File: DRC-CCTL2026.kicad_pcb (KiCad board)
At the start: 2 copper layers, 80 x 60 mm, 75 parts, among them J1 USB_C, J10 SW3, J12 LCD_BackLight, J2 FDCAN1, J3 FDCAN2, J4 FDCAN3, J5 SW1, J6 SW2, J7 STLINK, J8 I2C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

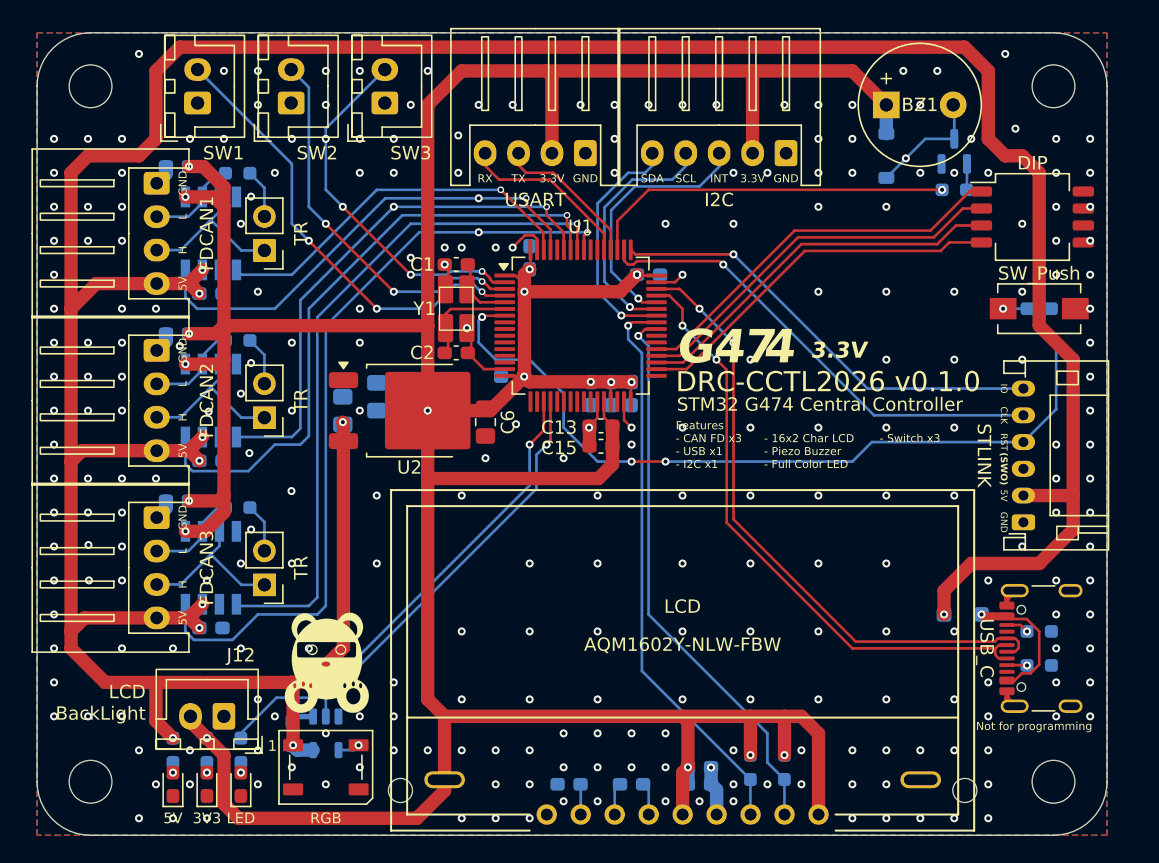
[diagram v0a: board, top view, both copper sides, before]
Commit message: T字配線にフィレットを追加
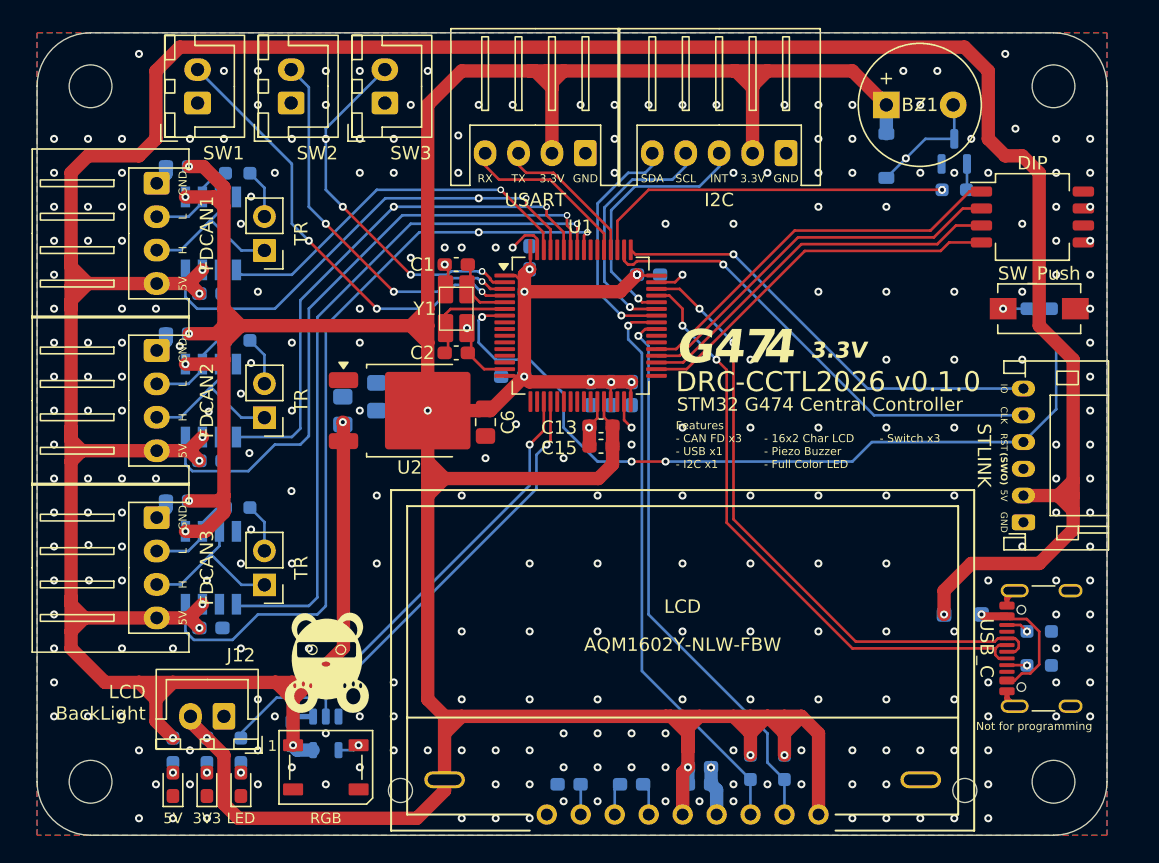
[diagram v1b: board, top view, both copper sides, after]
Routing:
- net +3V3: track 302.0 -> 334.4 mm
- net +5V: track 252.6 -> 271.5 mm

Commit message: 不要なビアを削除
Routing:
- net Net-(BZ1--): vias 1 -> 0
- net /SW3: vias 4 -> 3
- net /FDCAN3_RX: vias 2 -> 1
- net /FDCAN2_TX: vias 2 -> 1
- net /FDCAN1_RX: vias 2 -> 1
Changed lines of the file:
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@@
 		(net 47)
-	)
-	(via
-		(at 174.96 79.39)
-		(size 0.6)
-		(drill 0.3)
-		(layers "F.Cu" "B.Cu")
-		(net 50)
 	)
 	(segment
@@
 		(at 146.576 82.375)
 		(size 0.5)
-		(drill 0.3)
-		(layers "F.Cu" "B.Cu")
-		(net 53)
-	)
-	(via
-		(at 143.02 82.375)
-		(size 0.6)
 		(drill 0.3)
 		(layers "F.Cu" "B.Cu")
@@
 		(net 57)
 	)
-	(via
-		(at 136.67 83.01)
-		(size 0.6)
-		(drill 0.3)
-		(layers "F.Cu" "B.Cu")
-		(net 57)
-	)
 	(segment
 		(start 129.05 100.225)
@@
 		(width 0.2)
 		(layer "F.Cu")
-		(net 62)
-	)
-	(via
-		(at 143.02 84.915)
-		(size 0.6)
-		(drill 0.3)
-		(layers "F.Cu" "B.Cu")
 		(net 62)
 	)
@@
 		(size 0.6)
 		(drill 0.3)
-		(layers "F.Cu" "B.Cu")
-		(net 67)
-	)
-	(via
-		(at 131.59 77.93)
-		(size 0.6)
-		(drill 0.3)

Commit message: 配線を改善
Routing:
- net GND: vias 270 -> 268
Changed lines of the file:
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@@
 	)
 	(via
-		(at 158.26 119.84)
-		(size 0.6)
-		(drill 0.3)
-		(layers "F.Cu" "B.Cu")
-		(free yes)
-		(net 1)
-	)
-	(via
 		(at 118.89 126.19)
 		(size 0.6)
@@
 	)
 	(via
-		(at 162.07 123.65)
-		(size 0.6)
-		(drill 0.3)
-		(layers "F.Cu" "B.Cu")
-		(free yes)
-		(net 1)
-	)
-	(via
 		(at 111.27 90.63)
 		(size 0.6)
@@
 	)
 	(segment
-		(start 155.225 93.945)
-		(end 154.196 92.916)
+		(start 155.225 113.757)
+		(end 155.225 93.945)
 		(width 0.2)
 		(layer "B.Cu")
@@
 	(segment
 		(start 163.34 125.8325)
-		(end 155.225 117.7175)
+		(end 163.34 128.441)
+		(width 0.2)
+		(layer "B.Cu")
+		(net 30)
+	)
+	(segment
+		(start 154.196 92.916)
+		(end 154.196 91.9)
 		(width 0.2)
 		(layer "B.Cu")
@@
 	(segment
 		(start 163.34 125.8325)
-		(end 163.34 128.441)
+		(end 162.451 124.9435)
 		(width 0.2)
 		(layer "B.Cu")
@@
 	)
 	(segment
-		(start 154.196 92.916)
-		(end 154.196 91.9)
+		(start 163.34 128.441)
+		(end 163.35 128.451)
 		(width 0.2)
 		(layer "B.Cu")
@@
 	)
 	(segment
-		(start 155.225 117.7175)
-		(end 155.225 93.945)
+		(start 155.225 93.945)
+		(end 154.196 92.916)
 		(width 0.2)
 		(layer "B.Cu")
@@
 	)
 	(segment
-		(start 163.34 128.441)
-		(end 163.35 128.451)
+		(start 162.451 124.9435)
+		(end 162.451 120.983)
+		(width 0.2)
+		(layer "B.Cu")
+		(net 30)
+	)
+	(segment
+		(start 162.451 120.983)
+		(end 155.225 113.757)
 		(width 0.2)
 		(layer "B.Cu")

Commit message: ledの抵抗値を変更
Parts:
- R3, R5: value 1k -> 470
- R4: value 2.2k -> 1k
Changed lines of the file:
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@@
 			)
 		)
-		(property "Value" "1k"
+		(property "Value" "470"
 			(at 0 -1.43 90)
 			(layer "B.Fab")
@@
 			)
 		)
-		(property "Value" "2.2k"
+		(property "Value" "1k"
 			(at 0 -1.43 90)
 			(layer "B.Fab")
@@
 			)
 		)
-		(property "Value" "1k"
+		(property "Value" "470"
 			(at 0 -1.43 90)
 			(layer "B.Fab")

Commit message: バージョンを変更
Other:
- board text added: "DRC-CCTL2026 v0.0.1"
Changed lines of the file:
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@@
 		)
 	)
-	(gr_text "DRC-CCTL2026 v0.1.0\n"
+	(gr_text "DRC-CCTL2026 v0.0.1"
 		(at 157.752 96.98 0)
 		(layer "F.SilkS")
@@
 			(justify left bottom)
 		)
-		(render_cache "DRC-CCTL2026 v0.1.0\n" 0
+		(render_cache "DRC-CCTL2026 v0.0.1" 0
 			(polygon
 				(pts
@@
 			(polygon
 				(pts
-					(xy 177.971735 96.78948) (xy 177.987118 96.786546) (xy 177.997903 96.777735) (xy 178.003243 96.758064)
-					(xy 178.003243 96.648796) (xy 177.999831 96.625451) (xy 177.991728 96.617227) (xy 177.975948 96.613167)
-					(xy 177.868706 96.600734) (xy 177.839345 96.58978) (xy 177.821759 96.573143) (xy 177.810446 96.535192)
-					(xy 177.807879 96.499594) (xy 177.80323 96.373921) (xy 177.801651 96.308352) (xy 177.804986 95.815323)
-					(xy 177.816606 95.42677) (xy 177.826838 95.280517) (xy 177.828945 95.246903) (xy 177.825934 95.225172)
-					(xy 177.816585 95.214094) (xy 177.801651 95.211182) (xy 177.780585 95.213289) (xy 177.660179 95.231333)
-					(xy 177.557761 95.240329) (xy 177.463496 95.24269) (xy 177.423654 95.24269) (xy 177.411266 95.245783)
-					(xy 177.401893 95.255715) (xy 177.398467 95.27209) (xy 177.397448 95.33061) (xy 177.39636 95.393907)
-					(xy 177.400562 95.421956) (xy 177.408764 95.427807) (xy 177.423654 95.429535) (xy 177.536701 95.433619)
-					(xy 177.560588 95.440019) (xy 177.57063 95.450478) (xy 177.572765 95.467454) (xy 177.576886 95.730229)
-					(xy 177.568015 96.275341) (xy 177.558018 96.5017) (xy 177.550134 96.558918) (xy 177.535505 96.585862)
-					(xy 177.50343 96.598421) (xy 177.433873 96.60805) (xy 177.371173 96.61106) (xy 177.359798 96.617239)
-					(xy 177.350046 96.630936) (xy 177.348 96.642568) (xy 177.349465 96.717454) (xy 177.350107 96.745424)
-					(xy 177.353117 96.769396) (xy 177.362467 96.784565) (xy 177.377401 96.78948) (xy 177.381614 96.78948)
-					(xy 177.681941 96.783251) (xy 177.967522 96.78948)
+					(xy 177.727423 95.215209) (xy 177.775931 95.227539) (xy 177.820989 95.245022) (xy 177.86428 95.268403)
+					(xy 177.904013 95.296803) (xy 177.942732 95.332471) (xy 177.977582 95.373225) (xy 178.011463 95.423318)
+					(xy 178.040974 95.478641) (xy 178.068796 95.545644) (xy 178.091607 95.6179) (xy 178.111346 95.703751)
+					(xy 178.125393 95.794467) (xy 178.134614 95.899166) (xy 178.137607 96.007567) (xy 178.136487 96.072336)
+					(xy 178.119487 96.258903) (xy 178.085 96.416952) (xy 178.036839 96.54533) (xy 177.978048 96.645821)
+					(xy 177.910409 96.721384) (xy 177.834217 96.774762) (xy 177.748318 96.807411) (xy 177.700871 96.815901)
+					(xy 177.650434 96.818789) (xy 177.559193 96.811126) (xy 177.509522 96.799422) (xy 177.463608 96.782676)
+					(xy 177.420053 96.760361) (xy 177.380254 96.733188) (xy 177.341808 96.699143) (xy 177.307347 96.66018)
+					(xy 177.273916 96.612101) (xy 177.244914 96.558884) (xy 177.217391 96.493551) (xy 177.194918 96.422859)
+					(xy 177.175108 96.336512) (xy 177.161081 96.244837) (xy 177.151551 96.133761) (xy 177.148515 96.0181)
+					(xy 177.148551 96.015993) (xy 177.398467 96.015993) (xy 177.401863 96.148944) (xy 177.419483 96.313691)
+					(xy 177.448796 96.431876) (xy 177.486717 96.513672) (xy 177.531799 96.567668) (xy 177.585091 96.599662)
+					(xy 177.616228 96.60809) (xy 177.650434 96.610969) (xy 177.688585 96.606006) (xy 177.71689 96.594874)
+					(xy 177.74264 96.577802) (xy 177.769513 96.550967) (xy 177.793172 96.517237) (xy 177.817686 96.468112)
+					(xy 177.83793 96.410911) (xy 177.857164 96.331913) (xy 177.870838 96.244557) (xy 177.880481 96.132064)
+					(xy 177.883533 96.013886) (xy 177.880436 95.88003) (xy 177.86353 95.71123) (xy 177.835074 95.591837)
+					(xy 177.798018 95.509839) (xy 177.753707 95.455898) (xy 177.700957 95.423925) (xy 177.669888 95.415473)
+					(xy 177.635688 95.412591) (xy 177.59284 95.419048) (xy 177.564646 95.431493) (xy 177.538884 95.450032)
+					(xy 177.511893 95.478762) (xy 177.488027 95.514616) (xy 177.463508 95.565882) (xy 177.443155 95.625402)
+					(xy 177.424245 95.705058) (xy 177.410693 95.793122) (xy 177.40146 95.901469) (xy 177.398467 96.015993)
+					(xy 177.148551 96.015993) (xy 177.149541 95.957414) (xy 177.166536 95.771827) (xy 177.201475 95.613066)
+					(xy 177.250399 95.483294) (xy 177.310005 95.381435) (xy 177.378226 95.304885) (xy 177.454478 95.250981)
+					(xy 177.539631 95.218167) (xy 177.586276 95.209674) (xy 177.635688 95.206786)
 				)
 			)
@@
 			(polygon
 				(pts
-					(xy 179.468386 95.215209) (xy 179.516894 95.227539) (xy 179.561952 95.245022) (xy 179.605243 95.268403)
-					(xy 179.644976 95.296803) (xy 179.683695 95.332471) (xy 179.718545 95.373225) (xy 179.752426 95.423318)
-					(xy 179.781937 95.478641) (xy 179.809759 95.545644) (xy 179.83257 95.6179) (xy 179.852309 95.703751)
-					(xy 179.866356 95.794467) (xy 179.875577 95.899166) (xy 179.87857 96.007567) (xy 179.87745 96.072336)
-					(xy 179.86045 96.258903) (xy 179.825963 96.416952) (xy 179.777802 96.54533) (xy 179.719011 96.645821)
-					(xy 179.651372 96.721384) (xy 179.57518 96.774762) (xy 179.489281 96.807411) (xy 179.441834 96.815901)
-					(xy 179.391397 96.818789) (xy 179.300156 96.811126) (xy 179.250485 96.799422) (xy 179.204571 96.782676)
-					(xy 179.161016 96.760361) (xy 179.121217 96.733188) (xy 179.082771 96.699143) (xy 179.04831 96.66018)
-					(xy 179.014879 96.612101) (xy 178.985877 96.558884) (xy 178.958354 96.493551) (xy 178.935881 96.422859)
-					(xy 178.916071 96.336512) (xy 178.902044 96.244837) (xy 178.892514 96.133761) (xy 178.889478 96.0181)
-					(xy 178.889514 96.015993) (xy 179.13943 96.015993) (xy 179.142826 96.148944) (xy 179.160446 96.313691)
-					(xy 179.189759 96.431876) (xy 179.22768 96.513672) (xy 179.272762 96.567668) (xy 179.326054 96.599662)
-					(xy 179.357191 96.60809) (xy 179.391397 96.610969) (xy 179.429548 96.606006) (xy 179.457853 96.594874)
-					(xy 179.483603 96.577802) (xy 179.510476 96.550967) (xy 179.534135 96.517237) (xy 179.558649 96.468112)
-					(xy 179.578893 96.410911) (xy 179.598127 96.331913) (xy 179.611801 96.244557) (xy 179.621444 96.132064)
-					(xy 179.624496 96.013886) (xy 179.621399 95.88003) (xy 179.604493 95.71123) (xy 179.576037 95.591837)
-					(xy 179.538981 95.509839) (xy 179.49467 95.455898) (xy 179.44192 95.423925) (xy 179.410851 95.415473)
-					(xy 179.376651 95.412591) (xy 179.333803 95.419048) (xy 179.305609 95.431493) (xy 179.279847 95.450032)
-					(xy 179.252856 95.478762) (xy 179.22899 95.514616) (xy 179.204471 95.565882) (xy 179.184118 95.625402)
-					(xy 179.165208 95.705058) (xy 179.151656 95.793122) (xy 179.142423 95.901469) (xy 179.13943 96.015993)
-					(xy 178.889514 96.015993) (xy 178.890504 95.957414) (xy 178.907499 95.771827) (xy 178.942438 95.613066)
-					(xy 178.991362 95.483294) (xy 179.050968 95.381435) (xy 179.119189 95.304885) (xy 179.195441 95.250981)
-					(xy 179.280594 95.218167) (xy 179.327239 95.209674) (xy 179.376651 95.206786)
+					(xy 179.712698 96.78948) (xy 179.728081 96.786546) (xy 179.738866 96.777735) (xy 179.744206 96.758064)
+					(xy 179.744206 96.648796) (xy 179.740794 96.625451) (xy 179.732691 96.617227) (xy 179.716911 96.613167)
+					(xy 179.609669 96.600734) (xy 179.580308 96.58978) (xy 179.562722 96.573143) (xy 179.551409 96.535192)
+					(xy 179.548842 96.499594) (xy 179.544193 96.373921) (xy 179.542614 96.308352) (xy 179.545949 95.815323)
+					(xy 179.557569 95.42677) (xy 179.567801 95.280517) (xy 179.569908 95.246903) (xy 179.566897 95.225172)
+					(xy 179.557548 95.214094) (xy 179.542614 95.211182) (xy 179.521548 95.213289) (xy 179.401142 95.231333)
+					(xy 179.298724 95.240329) (xy 179.204459 95.24269) (xy 179.164617 95.24269) (xy 179.152229 95.245783)
+					(xy 179.142856 95.255715) (xy 179.13943 95.27209) (xy 179.138411 95.33061) (xy 179.137323 95.393907)
+					(xy 179.141525 95.421956) (xy 179.149727 95.427807) (xy 179.164617 95.429535) (xy 179.277664 95.433619)
+					(xy 179.301551 95.440019) (xy 179.311593 95.450478) (xy 179.313728 95.467454) (xy 179.317849 95.730229)
+					(xy 179.308978 96.275341) (xy 179.298981 96.5017) (xy 179.291097 96.558918) (xy 179.276468 96.585862)
+					(xy 179.244393 96.598421) (xy 179.174836 96.60805) (xy 179.112136 96.61106) (xy 179.100761 96.617239)
+					(xy 179.091009 96.630936) (xy 179.088963 96.642568) (xy 179.090428 96.717454) (xy 179.09107 96.745424)
+					(xy 179.09408 96.769396) (xy 179.10343 96.784565) (xy 179.118364 96.78948) (xy 179.122577 96.78948)
+					(xy 179.422904 96.783251) (xy 179.708485 96.78948)
 				)
 			)
@@
 			(keep_text_aligned yes)
 		)
-		(gr_text "3150"
+		(gr_text "80.01"
 			(at 150.005 56.46 0)
 			(layer "Dwgs.User")
@@
 			(keep_text_aligned yes)
 		)
-		(gr_text "2362.2047"
+		(gr_text "60"
 			(at 96.15 100 90)
 			(layer "Dwgs.User")

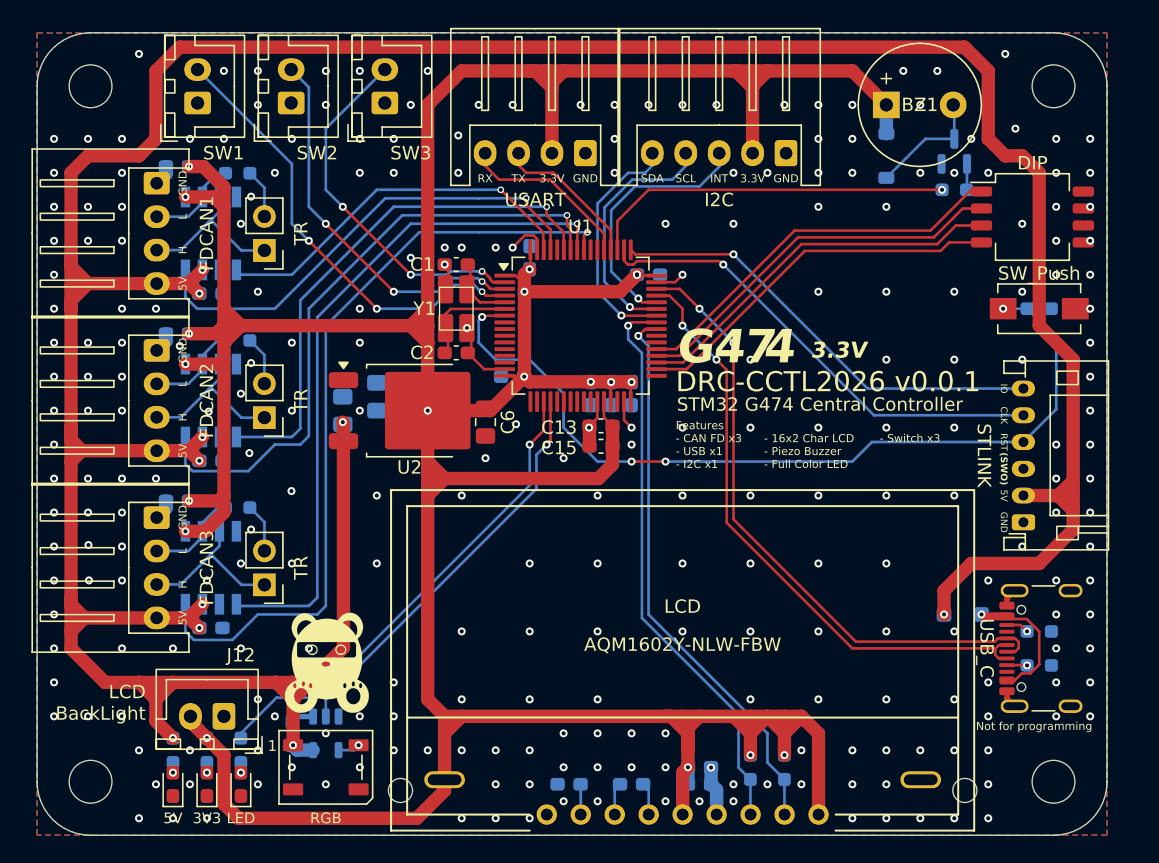
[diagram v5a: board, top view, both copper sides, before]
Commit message: パターン引き直し・部品配置変更
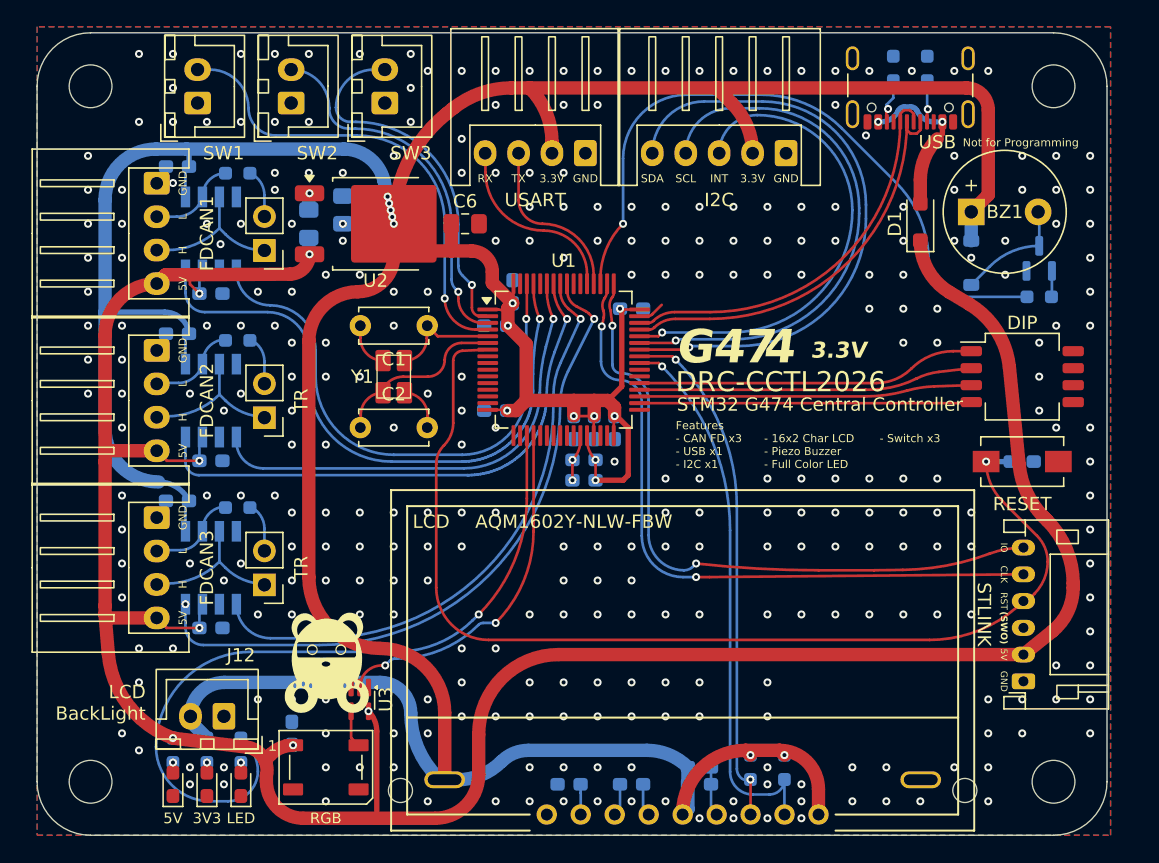
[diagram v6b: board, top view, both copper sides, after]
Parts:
- C1, C2: value 12p -> 10p; footprint Capacitor_SMD:C_0603_1608Metric_Pad1.08x0.95mm_HandSolder -> Capacitor_THT:C_Disc_D5.0mm_W2.5mm_P5.00mm
- C13, C15: moved to B.Cu
- D1: moved to F.Cu
- J1: value USB_C -> USB
- SW1: value SW_Push -> RESET
- U3: value 74AHCT1G125 -> 74AHC1G125; footprint lib:SOT95P280X145-5N -> Package_TO_SOT_SMD:SOT-353_SC-70-5; moved to F.Cu
- moved R1 45.4 mm to (176.6, 72.7), turned to 90 degrees
- moved J1 44.4 mm to (175.3, 73.0), turned to 180 degrees
- moved R2 43.5 mm to (174.0, 72.7), turned to 90 degrees
- moved D1 29.5 mm to (176.0, 84.2), turned to 90 degrees
- moved C6 14.9 mm to (142.0, 84.3), turned to 0 degrees
- moved C4 14.2 mm to (130.3, 84.3)
- moved C5 14.2 mm to (132.9, 83.2)
- moved U2 14.2 mm to (135.4, 84.3)
- moved SW2 12.0 mm to (183.7, 95.7)
- moved J7 11.9 mm to (183.8, 118.5)
- moved C3 11.5 mm to (183.7, 102.1)
- moved SW1 11.5 mm to (183.7, 102.1)
- moved BZ1 10.2 mm to (182.3, 83.4)
- moved D6 10.2 mm to (179.8, 87.2)
- moved Q1 10.2 mm to (184.9, 86.9)
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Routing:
- net +5V: track 271.5 -> 195.5 mm, vias 10 -> 7
- net /I2C_SDA: track 17.9 -> 45.3 mm
- net /BUZZER: track 27.4 -> 50.3 mm
- net /I2C_SCL: track 18.6 -> 40.6 mm
- net /LED_BI: track 36.3 -> 56.8 mm
- net /USB_D_P: track 47.5 -> 29.7 mm, vias 2 -> 0
- net /NRST: track 64.0 -> 81.5 mm, vias 4 -> 1
- net /I2C_INT: track 19.4 -> 36.1 mm
- net /SWDIO: track 33.7 -> 50.1 mm, vias 1 -> 2
- net /USB_D_N: track 46.2 -> 30.4 mm, vias 2 -> 0
- net /SWCLK: track 35.7 -> 50.8 mm, vias 1 -> 2
- net GND: track 30.9 -> 17.5 mm, vias 268 -> 318
- net /FDCAN1_TX: track 28.4 -> 40.5 mm
- net /FDCAN1_RX: track 35.9 -> 46.4 mm
- net +3V3: track 334.4 -> 325.8 mm, vias 20 -> 17
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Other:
- board text added: "DRC-CCTL2026"
- board text added: "DRC-CCTL2026 v0.0.2"
- board text added: "Not for Programming"
- board text removed: "DRC-CCTL2026 v0.0.1"
- board text removed: "DRC-CCTL2026 v0.1.0"
- board text removed: "Not for programming"
